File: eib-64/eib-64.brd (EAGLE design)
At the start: 15.2 x 17.2 mm, 25 parts, among them J1 DF40-REC

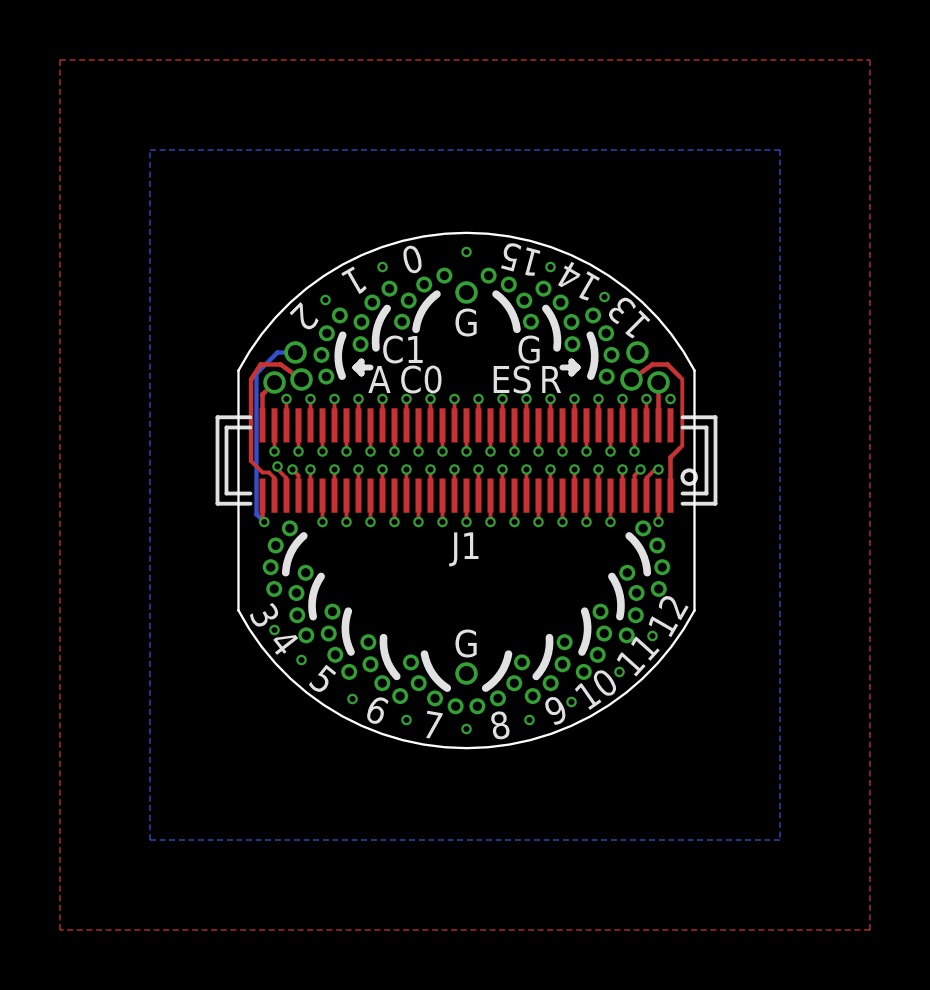
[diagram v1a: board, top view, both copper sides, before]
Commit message: Reduced size of eib-64
- Also created v-cut panelized board with 12 eibs
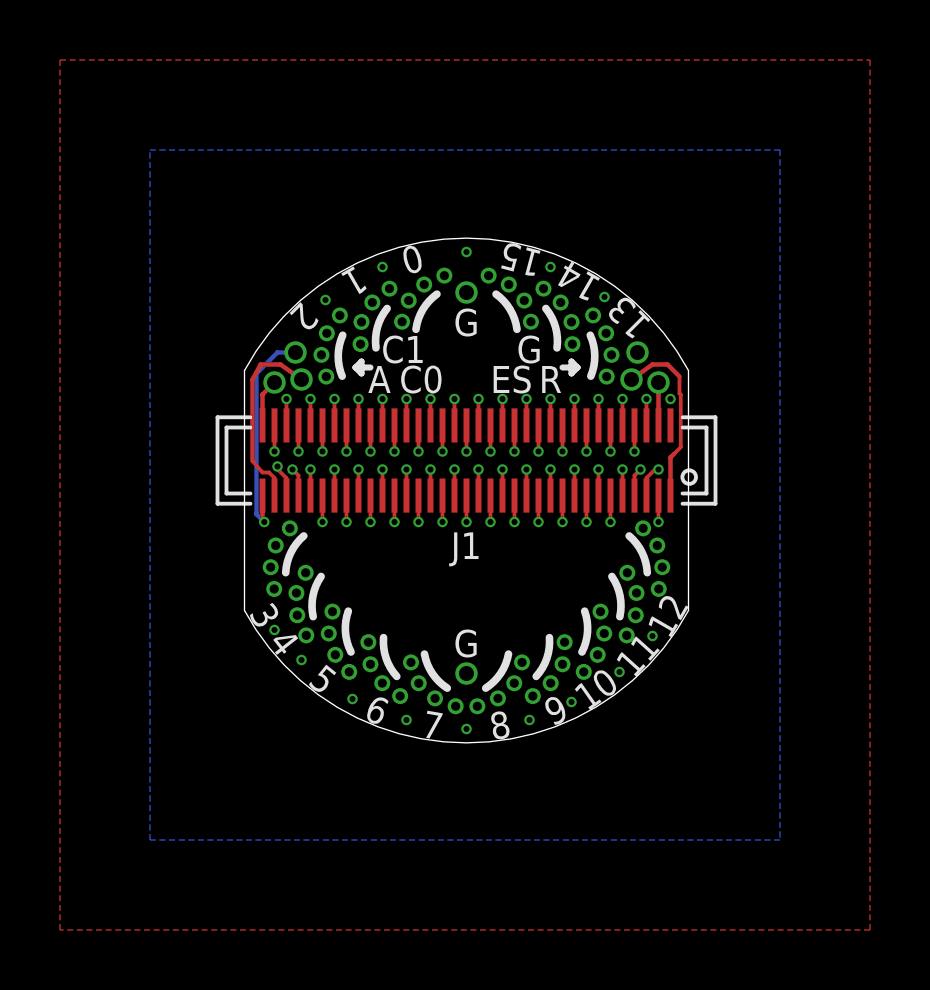
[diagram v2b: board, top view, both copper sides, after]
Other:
- board size 15.2 x 17.2 mm -> 14.8 x 16.8 mm

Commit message: Updated eib-64 to meet seeed low-cost spec
- 8 mil trace/pour spacing
- Added stencil gerbers as well
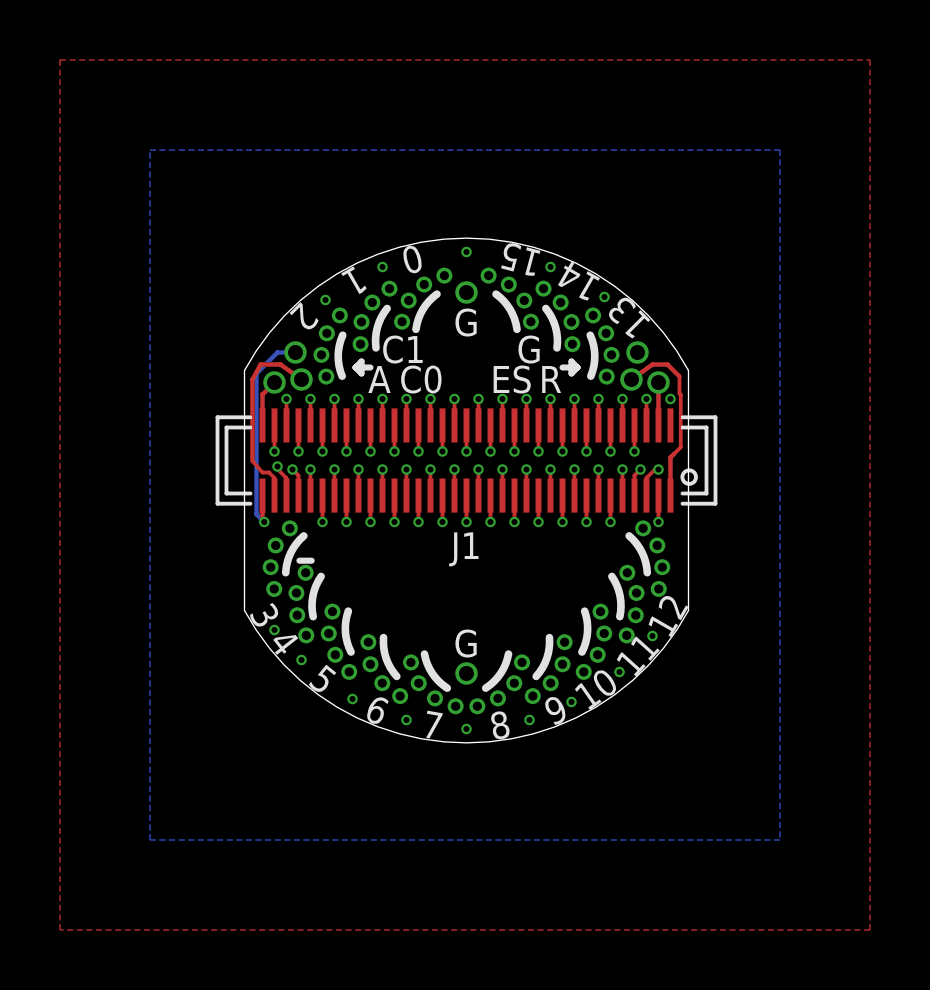
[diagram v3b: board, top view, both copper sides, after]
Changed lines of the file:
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@@
 <setting verticaltext="up"/>
 </settings>
-<grid distance="0.1" unitdist="mm" unit="mm" style="lines" multiple="1" display="yes" altdistance="5" altunitdist="mil" altunit="mil"/>
+<grid distance="0.01" unitdist="mm" unit="mm" style="lines" multiple="1" display="yes" altdistance="5" altunitdist="mil" altunit="mil"/>
 <layers>
 <layer number="1" name="Top" color="4" fill="1" visible="yes" active="yes"/>
@@
 <layer number="14" name="Route14" color="1" fill="6" visible="no" active="no"/>
 <layer number="15" name="Route15" color="4" fill="6" visible="yes" active="yes"/>
-<layer number="16" name="Bottom" color="1" fill="1" visible="yes" active="yes"/>
+<layer number="16" name="Bottom" color="1" fill="1" visible="no" active="yes"/>
 <layer number="17" name="Pads" color="2" fill="1" visible="yes" active="yes"/>
 <layer number="18" name="Vias" color="2" fill="1" visible="yes" active="yes"/>
@@
 <wire x1="-7.4" y1="4" x2="-7.4" y2="-4" width="0" layer="20"/>
 <wire x1="7.4" y1="4" x2="7.4" y2="-4" width="0" layer="20"/>
+<wire x1="-5.57" y1="-2.34" x2="-5.16" y2="-2.34" width="0.2032" layer="21"/>
 </plain>
 <attributes>
@@
 <contactref element="GND0" pad="P$1"/>
 <contactref element="GND1" pad="P$1"/>
-<polygon width="0.127" layer="16" thermals="no">
+<polygon width="0.127" layer="16" isolate="0.2032" thermals="no">
 <vertex x="-10.549996875" y="11.349996875"/>
 <vertex x="10.449996875" y="11.349996875"/>
@@
 <vertex x="-10.549996875" y="-11.649996875"/>
 </polygon>
-<polygon width="0.127" layer="1" thermals="no">
+<polygon width="0.127" layer="1" isolate="0.2032" thermals="no">
 <vertex x="-13.549996875" y="14.35"/>
 <vertex x="13.45" y="14.349996875"/>
@@
 <vertex x="-13.55" y="-14.649996875"/>
 </polygon>
-<polygon width="0.127" layer="15" thermals="no">
+<polygon width="0.127" layer="15" isolate="0.2032" thermals="no">
 <vertex x="-11.549996875" y="12.349996875"/>
 <vertex x="11.449996875" y="12.349996875"/>
@@
 <vertex x="-11.549996875" y="-12.649996875"/>
 </polygon>
-<polygon width="0.127" layer="2" thermals="no">
+<polygon width="0.127" layer="2" isolate="0.2032" thermals="no">
 <vertex x="-12.549996875" y="13.35"/>
 <vertex x="12.45" y="13.349996875"/>

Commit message: eib-64 rev. 1.1
- Fits latest shuttle drive reatining feature.
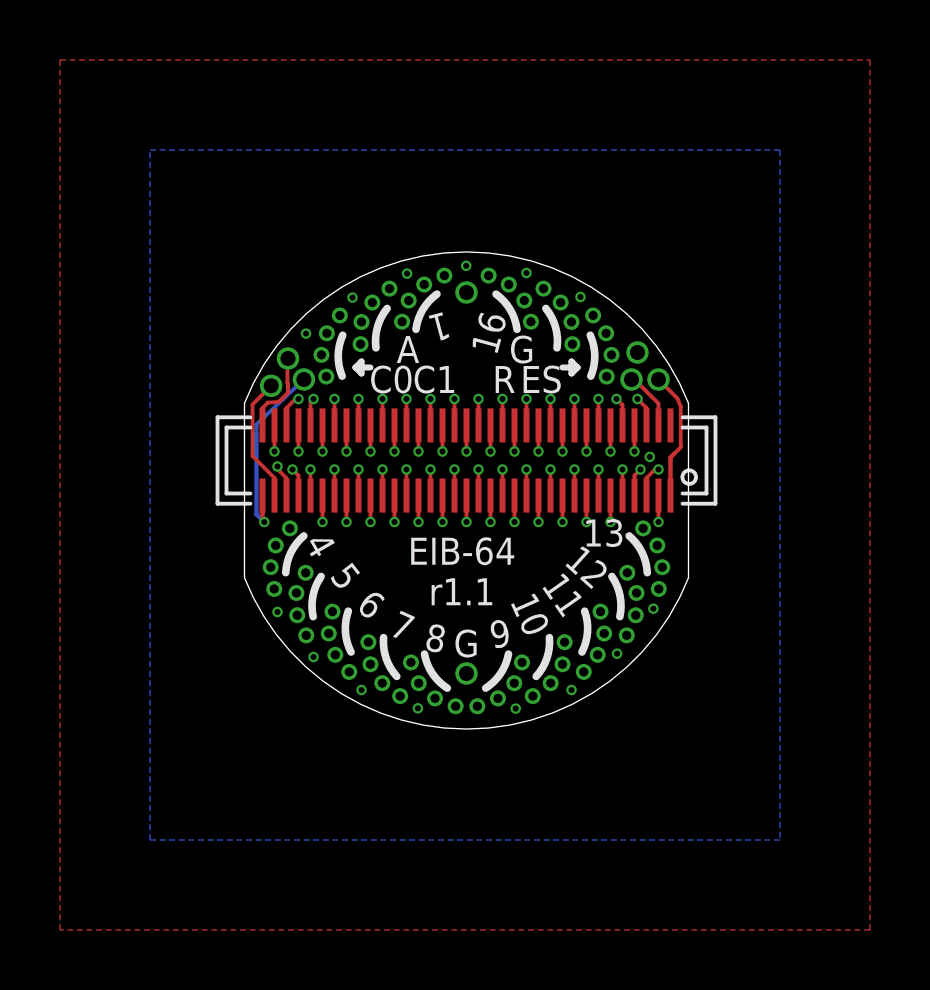
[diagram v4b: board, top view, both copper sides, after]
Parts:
- moved CAT0 1.03 mm to (-6.51, 3.49)
- moved CAT1 0.94 mm to (-5.42, 3.70)
- moved AN 0.92 mm to (-5.95, 4.40)
- moved REF 0.91 mm to (5.50, 3.70)
- moved ESTIM 0.90 mm to (6.40, 3.70)
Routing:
- net CAT0: track 6.38 -> 4.22 mm
- net ESTIM: track 6.05 -> 4.29 mm
- net AN: track 1.60 -> 2.79 mm
- net CAT1: track 7.55 -> 6.44 mm
- net REF: track 1.43 -> 1.96 mm
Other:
- board size 14.8 x 16.8 mm -> 14.8 x 15.9 mm
- board text added: "16"
- board text added: "EIB-64 r1.1"
- board text removed: "0"
- board text removed: "14"
- board text removed: "15"
- board text removed: "2"
- board text removed: "3"

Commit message: Updates to eib-64 for latest shuttle drives
- Decreased outer diameter
- Removed flat spots because they are not required anymore (headstage
retention clips were removed from drive body design)
- Remade panel and added labelled fiducial marks as per Filipe's
requirments
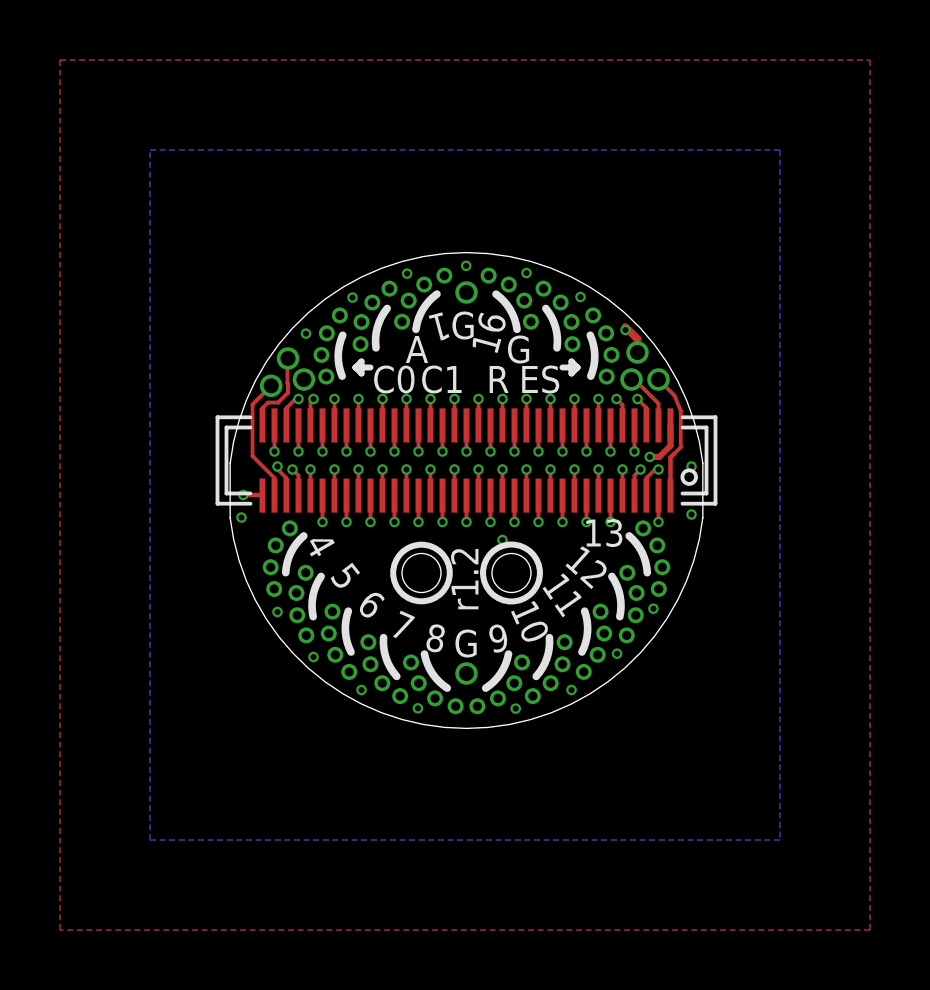
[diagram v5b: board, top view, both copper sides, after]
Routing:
- net GND: track 0.00 -> 2.54 mm, vias 15 -> 20
- net CAT1: track 6.44 -> 5.35 mm
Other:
- board size 14.8 x 15.9 mm -> 15.8 x 15.9 mm
- board text added: "EIB-64 r1.2 JPN '19 OHL v1.2"
- board text added: "r1.2"
- board text removed: "EIB-64 JPN '17 OHL v1.2"
- board text removed: "EIB-64 r1.1"

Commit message: Address Filipe's issues with eib-64 prior to fabrication
- Move mouse bites on panel away from connector since it will be hard to
sand under there.
- Reduce ground planes around mouse bites to prvent exposued copper
after sanding.
- Adde "Open Ephys" to bottom silk.
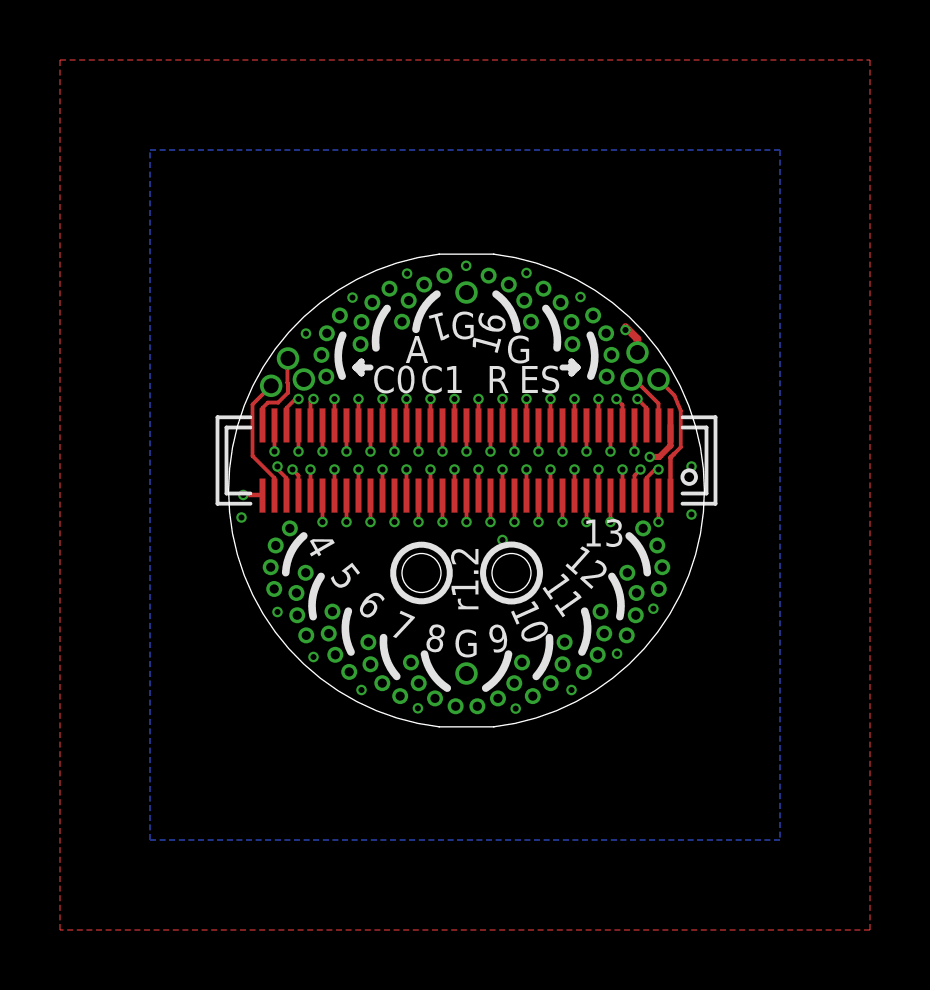
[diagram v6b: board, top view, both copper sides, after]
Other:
- board size 15.8 x 15.9 mm -> 15.9 x 15.8 mm
- board text added: "EIB-64, r1.2 JPN & Open Ephys OHL v1.2 '19"
- board text removed: "EIB-64 r1.2 JPN '19 OHL v1.2"

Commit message: headstage-64 rev. 1.4 along with all dependencies
- This is headstage-64 revision 1.4. Because it involves a change in the
bottom analog connector, a lot of other boards had to be changed to
match the new pinout. That is why there are so many files in this
commit. Changes in revision 1.4 and affects on other boards are as
follows:

1. The coaxial adapter board has been improved to allow a regulator to
sit on the daughter board. To do this, the filtered vcoax had to brought
back to the daughter board and then out again after regulation. Of
course this regulation can be bypassed simply by connecting these
contacts

2. Vcoax decoupling has been greatly improved to lower impedance of
power input. There is now 70 uF of decoupling capacitance on the
post-regulated vcoax.

3. The JTAG interface was changed to allow it to be enabled and disabled
by the programmer. This means that these pins are nominally used for
extra IO. The programmer now contains a jumper that allows it operate in
this new mode (closed) or legacy mode (open) for headstage-64 rev 1.3.

4. All of the serializers GPIO lines are now all routed to the FPGA.

5. The opto and estim circuits no longer share SPI lines so they can be
operated independently.

6. The analog routing to the intan chip has been changed such that the
electrode lines are shielded from vcoax, which was polluting the anlog
signals, by a ground pin. This means that eibs etc. need to respect this
new pinout. This is why eib-64, eib-64-large, nanoz-adapter,
omnetics-adapter-64, and test-board-64 have been changed.

7. The serializer on headstage-64 has been upgraded to DS90UB933-Q1
which has reduced back channel latencies, increased forward channel
bandwidth, and improved performance with
imperfect cabling.

8. There is a solder jumper on the bottom of headstage-64 to allow the
addition of an external resistor to AUXIN3 on the intan to allow it to
operate at lower bandwidths. This comes at the cost of not being able to
measure istim unless t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
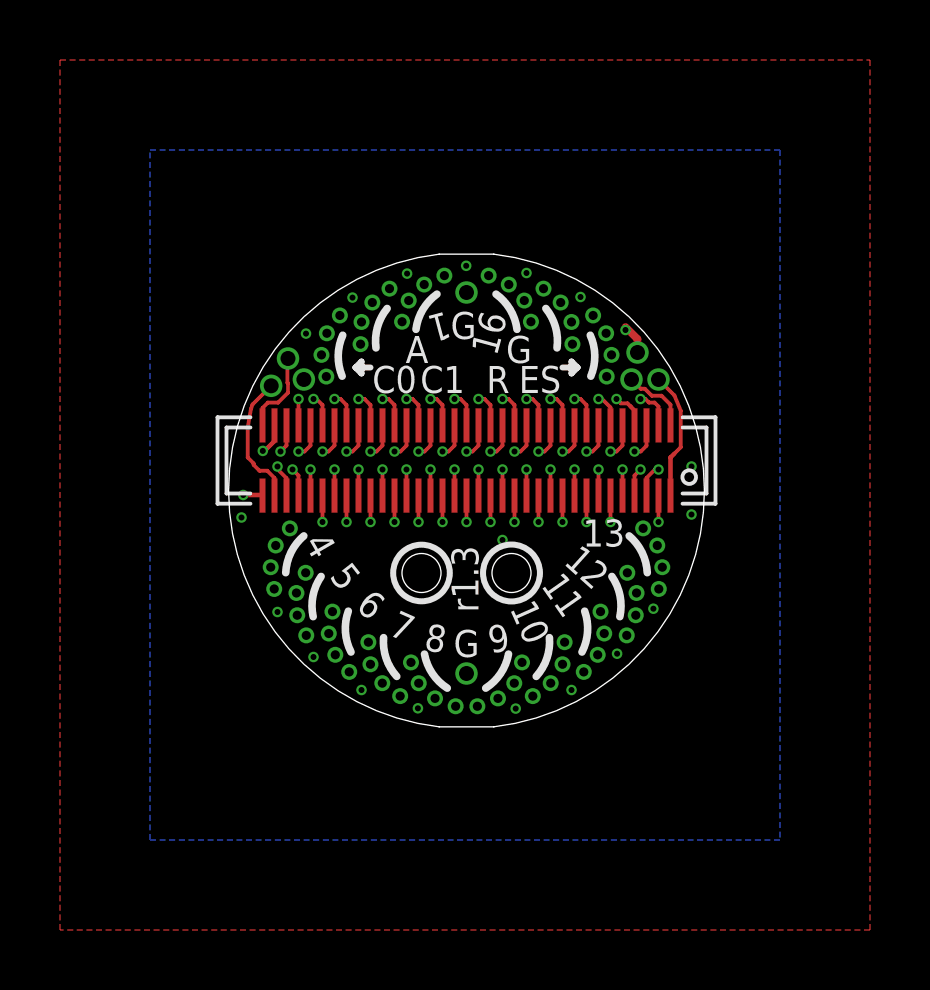
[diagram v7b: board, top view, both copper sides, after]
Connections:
- net GND: now also J1.37; no longer J1.70
- net N$1: now also J1.69; no longer J1.68
- net N$10: now also J1.60; no longer J1.59
- net N$11: now also J1.59; no longer J1.58
- net N$12: now also J1.58; no longer J1.57
- net N$13: now also J1.57; no longer J1.56
- net N$14: now also J1.56; no longer J1.55
- net N$15: now also J1.55; no longer J1.54
- net N$16: now also J1.54; no longer J1.53
- net N$17: now also J1.53; no longer J1.52
- net N$18: now also J1.52; no longer J1.51
- net N$19: now also J1.51; no longer J1.50
- net N$2: now also J1.66; no longer J1.65
- net N$20: now also J1.50; no longer J1.49
- net N$21: now also J1.49; no longer J1.48
- net N$22: now also J1.48; no longer J1.47
- net N$23: now also J1.47; no longer J1.46
- net N$24: now also J1.46; no longer J1.45
- net N$25: now also J1.45; no longer J1.44
- net N$26: now also J1.44; no longer J1.43
- net N$27: now also J1.43; no longer J1.42
- net N$28: now also J1.42; no longer J1.41
- net N$29: now also J1.41; no longer J1.40
- net N$3: now also J1.67; no longer J1.66
- net N$30: now also J1.40; no longer J1.39
- net N$31: now also J1.39; no longer J1.38
- net N$32: now also J1.38; no longer J1.37
- net N$4: now also J1.68; no longer J1.67
- net N$5: now also J1.65; no longer J1.64
- net N$6: now also J1.64; no longer J1.63
- net N$7: now also J1.63; no longer J1.62
- net N$8: now also J1.62; no longer J1.61
- net N$9: now also J1.61; no longer J1.60
- net REF: now also J1.70; no longer J1.69
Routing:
- net N$29: track 6.40 -> 7.07 mm
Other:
- board text added: "r1.3"
- board text removed: "r1.2"
